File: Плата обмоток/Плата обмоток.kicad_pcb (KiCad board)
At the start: 2 copper layers, 58 x 58 mm, 7 parts, among them J1 A_OUT, J2 B_OUT, J3 C_OUT, J4 Conn_01x02, J5 Conn_02x02_Odd_Even, J6 Conn_01x02, J7 Conn_01x02

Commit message: Добавил ножевые разъёмы
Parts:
- added J10: 4900, Connector_My:3551, B.Cu at (70.9, 81.8)
- added J11: 4900, Connector_My:3551, B.Cu at (60.5, 99.1)
- added J12: 4900, Connector_My:3551, B.Cu at (61.9, 104.7)
- added J13: 4900, Connector_My:3551, B.Cu at (65.0, 109.8)
- added J8: 4900, Connector_My:3551, B.Cu at (78.8, 77.6)
- added J9: 4900, Connector_My:3551, B.Cu at (74.2, 78.4)
- J1: value A_OUT -> 4900; footprint Connector_My:Power_Wire -> Connector_My:3551; moved to B.Cu
- J2: value B_OUT -> 4900; footprint Connector_My:Power_Wire -> Connector_My:3551; moved to B.Cu
- J3: value C_OUT -> 4900; footprint Connector_My:Power_Wire -> Connector_My:3551; moved to B.Cu
- moved J3 39.3 mm to (96.5, 83.1), turned to 45 degrees
- moved J2 23.1 mm to (93.2, 79.7), turned to 60 degrees
- moved J1 4.19 mm to (88.8, 77.9), turned to 75 degrees
- moved J4 0.51 mm to (84.1, 116.1)
- moved J6 0.51 mm to (102.9, 94.7)
- moved J7 0.51 mm to (97.8, 109.2)
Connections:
- J2 pad 1: B_OUT -> A_OUT
- J3 pad 1: C_OUT -> A_OUT
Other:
- outline, holes or cut-outs redrawn

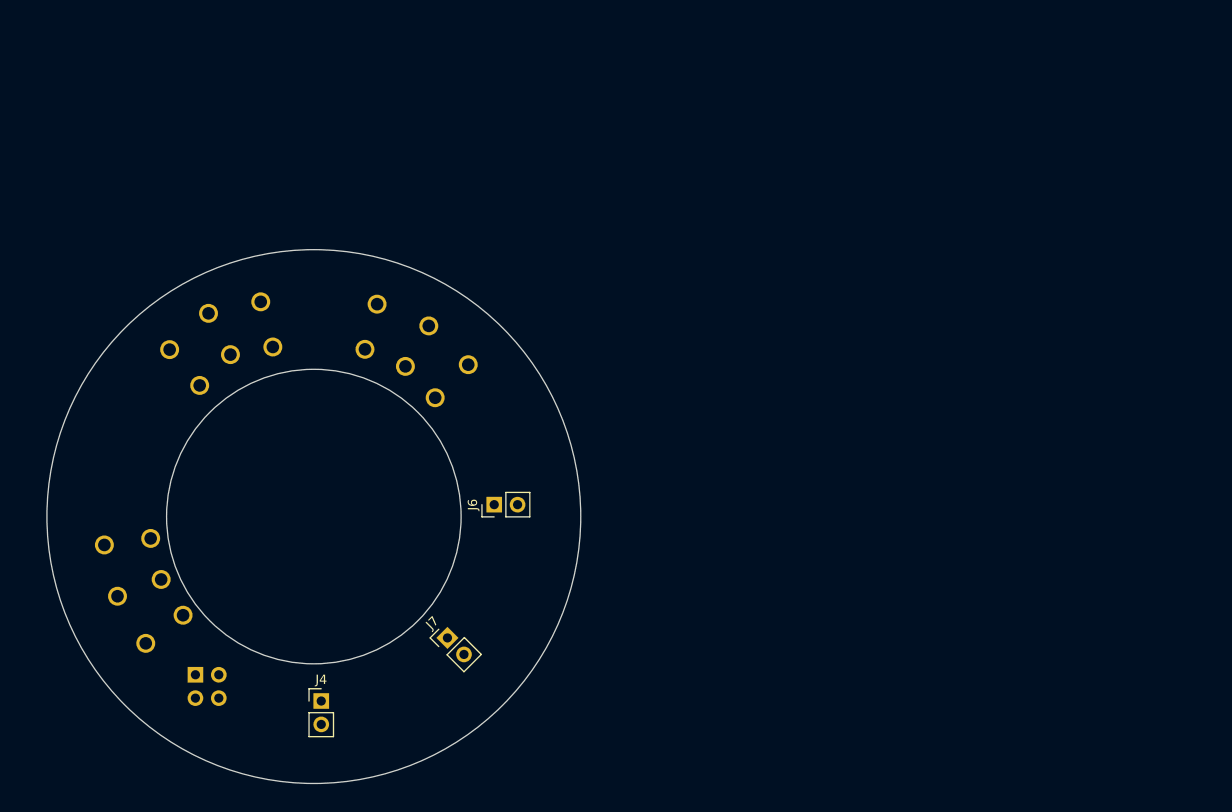
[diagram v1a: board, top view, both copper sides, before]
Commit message: Прямой вывод обмоток на плату
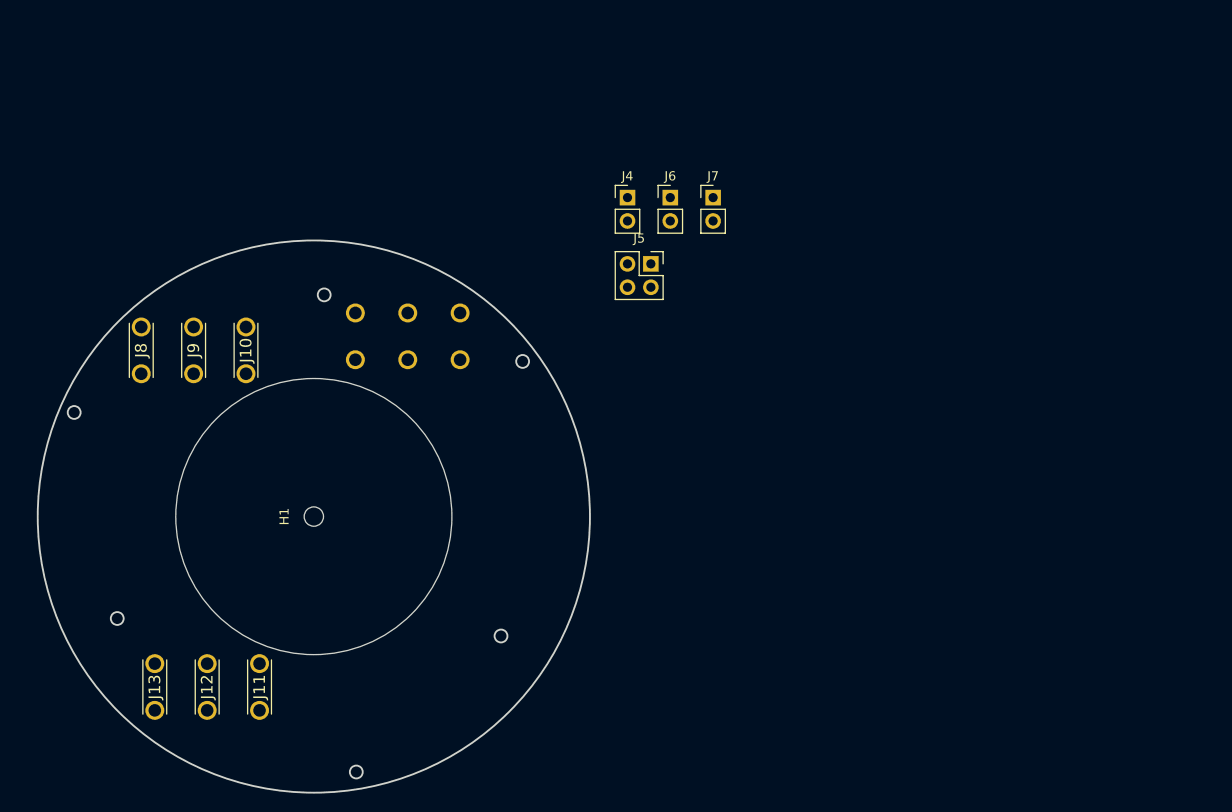
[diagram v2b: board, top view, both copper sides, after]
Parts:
- added H1: MountingHole, MountingHole:MountingHole_2.1mm, F.Cu at (83.3, 96.0)
- J10, J11, J12, J13, J5, J8, J9: moved to F.Cu
- moved J5 66.6 mm to (119.9, 68.6), turned to 0 degrees
- moved J4 64.0 mm to (117.3, 61.4)
- moved J7 55.9 mm to (126.6, 61.4), turned to 0 degrees
- moved J6 38.5 mm to (122.0, 61.4), turned to 0 degrees
- moved J11 21.2 mm to (77.4, 112.0), turned to -90 degrees
- moved J8 14.6 mm to (64.5, 80.5), turned to 90 degrees
- moved J12 12.2 mm to (71.7, 112.0), turned to -90 degrees
- moved J1 10.4 mm to (99.2, 79.0), turned to 90 degrees
- moved J3 9.60 mm to (87.8, 79.0), turned to 90 degrees
- moved J10 5.19 mm to (75.9, 80.5), turned to 90 degrees
- moved J9 4.51 mm to (70.2, 80.5), turned to 90 degrees
- moved J13 2.41 mm to (66.0, 112.0), turned to -90 degrees
- moved J2 0.77 mm to (93.5, 79.0), turned to 90 degrees
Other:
- board size 58 x 58 mm -> 60 x 60 mm
- board text added: "1"
- board text added: "2"
- board text added: "3"

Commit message: Расставил ножевые разъёмы финально
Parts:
- added J14: A1, Connector_My:Coil, F.Cu at (61.2, 86.4)
- added J15: A2, Connector_My:Coil, F.Cu at (87.1, 119.9)
- added J16: B1, Connector_My:Coil, F.Cu at (103.6, 109.0)
- added J17: B2, Connector_My:Coil, F.Cu at (102.6, 81.5)
- added J18: C1, Connector_My:Coil, F.Cu at (84.3, 71.9)
- added J19: C2, Connector_My:Coil, F.Cu at (62.0, 106.9)
- J10, J11, J12, J13, J5, J8, J9: moved to B.Cu
- moved J7 72.2 mm to (75.2, 112.0), turned to -25 degrees
- moved J5 67.2 mm to (67.0, 110.0), turned to 180 degrees
- moved J6 65.5 mm to (83.1, 114.0), turned to -5 degrees
- moved J4 64.7 mm to (79.0, 113.5), turned to -15 degrees
- moved J1 37.0 mm to (89.6, 114.7), turned to -70 degrees
- moved J2 33.3 mm to (94.2, 112.3), turned to -55 degrees
- moved J8 32.0 mm to (96.5, 82.1), turned to 45 degrees
- moved J3 31.4 mm to (98.0, 108.7), turned to -40 degrees
- moved J13 23.3 mm to (59.6, 89.6), turned to -15 degrees
- moved J9 22.3 mm to (92.5, 79.0), turned to 60 degrees
- moved J12 20.6 mm to (58.7, 96.0), turned to 0 degrees
- moved J11 20.2 mm to (59.6, 102.4), turned to 15 degrees
- moved J10 12.2 mm to (87.6, 77.1), turned to 75 degrees
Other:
- board size 60 x 60 mm -> 58 x 58 mm

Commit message: Финальная доработка
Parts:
- added H2: MountingHole, MountingHole:MountingHole_3.2mm_M3, F.Cu at (67.1, 81.3)
- added H3: MountingHole, MountingHole:MountingHole_3.2mm_M3, F.Cu at (80.8, 117.9)
- added H4: MountingHole, MountingHole:MountingHole_3.2mm_M3, F.Cu at (104.4, 89.9)
- J4, J6, J7: footprint Connector_PinHeader_2.54mm:PinHeader_1x02_P2.54mm_Vertical -> Connector_Molex:Molex_PicoBlade_53048-0210_1x02_P1.25mm_Horizontal; moved to B.Cu
- moved J6 40.1 mm to (72.1, 75.4), turned to -150 degrees
- moved J4 32.6 mm to (106.9, 96.6), turned to 90 degrees
- moved J7 5.76 mm to (72.3, 117.0), turned to -27 degrees
- turned J5 to 135 degrees
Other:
- outline, holes or cut-outs redrawn

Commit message: Ещё доработать
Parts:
- moved H3 43.9 mm to (90.2, 74.9)
- moved J9 43.8 mm to (71.9, 117.7)
- moved J5 43.3 mm to (97.8, 79.5)
- moved J8 42.8 mm to (76.7, 120.1), turned to 70 degrees
- moved J10 42.6 mm to (67.5, 114.7), turned to 50 degrees
- moved J17 41.7 mm to (61.2, 86.6)
- moved J15 40.1 mm to (103.6, 83.3)
- moved J6 36.3 mm to (105.4, 89.8), turned to 105 degrees
- moved J7 27.5 mm to (60.7, 92.1), turned to -95 degrees
- moved J19 27.3 mm to (85.9, 120.1)
- moved J11 25.6 mm to (67.0, 77.8), turned to -50 degrees
- moved J12 24.7 mm to (71.4, 74.8), turned to -60 degrees
- moved J13 23.9 mm to (76.3, 72.5), turned to -70 degrees
- moved J14 20.8 mm to (62.0, 107.2)
- moved H2 20.6 mm to (61.5, 101.1)
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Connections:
- J10 pad 1: B_OUT -> C_OUT
- J10 pad 2: B_OUT -> C_OUT
- J11 pad 1: C_OUT -> B_OUT
- J11 pad 2: C_OUT -> B_OUT
- J12 pad 1: C_OUT -> B_OUT
- J12 pad 2: C_OUT -> B_OUT
- J13 pad 1: C_OUT -> B_OUT
- J13 pad 2: C_OUT -> B_OUT
- J8 pad 1: B_OUT -> C_OUT
- J8 pad 2: B_OUT -> C_OUT
- J9 pad 1: B_OUT -> C_OUT
- J9 pad 2: B_OUT -> C_OUT
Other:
- board size 58 x 58 mm -> 61 x 58 mm

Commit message: Собираю документацию
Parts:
- removed H1: MountingHole, MountingHole:MountingHole_2.1mm
- moved J5 35.1 mm to (96.0, 114.6), turned to 180 degrees
- moved J1 26.3 mm to (109.7, 100.6), turned to 180 degrees
- moved J4 23.9 mm to (93.6, 76.3), turned to 155 degrees
- moved J3 23.9 mm to (109.7, 91.9), turned to 180 degrees
- moved J2 22.4 mm to (104.6, 96.3), turned to 0 degrees
- moved H4 22.1 mm to (88.4, 117.9)
- moved J6 9.29 mm to (100.5, 81.9), turned to 130 degrees
- moved J17 3.98 mm to (63.0, 83.1)
- moved J14 3.88 mm to (64.0, 110.5)
- moved J19 3.81 mm to (82.0, 120.1)
- moved H3 3.70 mm to (86.6, 73.9)
- moved J18 3.31 mm to (81.0, 72.1)
- moved J15 1.70 mm to (104.4, 84.8)
- moved J16 0.57 mm to (103.9, 108.5)
- moved J7 0.43 mm to (61.1, 92.1), turned to -100 degrees
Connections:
- J5 pad 2: PTC_Coil_C -> GNDA
- J5 pad 3: PTC_Coil_B -> PTC_Coil_C
- J5 pad 4: GNDA -> PTC_Coil_B
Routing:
- net PTC_Coil_C: track 0.00 -> 48.2 mm
- net PTC_Coil_A: track 0.00 -> 42.4 mm
- net PTC_Coil_B: track 0.00 -> 36.3 mm
- added copper zone on B.Cu, net A_OUT
- added copper zone on F.Cu, net A_OUT
- added copper zone on B.Cu, net B_OUT
- added copper zone on F.Cu, net B_OUT
- added copper zone on B.Cu, net C_OUT
- added copper zone on F.Cu, net C_OUT
- added copper zone on In2.Cu, net GNDA
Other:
- board size 61 x 58 mm -> 58 x 58 mm
- copper layers 2 -> 4
- board text removed: "1"
- board text removed: "3"

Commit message: Версия под отчётность
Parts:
- J14: renamed from J4; moved to F.Cu
- J16: renamed from J6; moved to F.Cu
- J19: renamed from J7; moved to F.Cu
- J5: renamed from J14; value A1 -> C2
- J6: renamed from J19; value C2 -> A1
- moved H3 15.5 mm to (101.4, 78.8)
- moved H2 12.3 mm to (59.3, 89.0)
- moved J16 9.98 mm to (96.3, 72.9), turned to -25 degrees
- moved J19 7.93 mm to (57.1, 98.9), turned to 100 degrees
- moved J14 7.51 mm to (89.2, 70.2), turned to -15 degrees
- moved J18 5.40 mm to (107.4, 104.4)
- moved J15 3.42 mm to (78.5, 69.8)
- moved J5 2.81 mm to (63.8, 113.3)
- moved H1 2.59 mm to (89.1, 120.3)
- renumbered H4 to H1, J12 to J10, J3 to J11, J10 to J12, J18 to J15, J15 to J17, J16 to J18, J8 to J2, J11 to J3, J5 to J4, J17 to J7, J2 to J8
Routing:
- net PTC_Coil_B: track 36.3 -> 48.8 mm
- net PTC_Coil_A: track 42.4 -> 52.2 mm
- net PTC_Coil_C: track 48.2 -> 49.9 mm
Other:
- outline, holes or cut-outs redrawn
- board text removed: "2"

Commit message: VER2.0
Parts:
- added J20: B1, Connector_My:temp_wire, B.Cu at (156.2, 97.3)
- added J21: B1, Connector_My:temp_wire, B.Cu at (145.4, 97.3)
- J14: value Conn_01x02 -> Conn_01x03; footprint Connector_Molex:Molex_PicoBlade_53048-0210_1x02_P1.25mm_Horizontal -> Connector_PinSocket_2.54mm:PinSocket_1x03_P2.54mm_Vertical; moved to B.Cu
- J15, J17, J18, J5, J6, J7: moved to B.Cu
- J16: value Conn_01x02 -> 4900; footprint Connector_Molex:Molex_PicoBlade_53048-0210_1x02_P1.25mm_Horizontal -> Connector_My:3551; moved to B.Cu
- J19: value Conn_01x02 -> B1; footprint Connector_Molex:Molex_PicoBlade_53048-0210_1x02_P1.25mm_Horizontal -> Connector_My:temp_wire; moved to B.Cu
- J4: value Conn_02x02_Odd_Even -> B1; footprint Connector_PinSocket_2.54mm:PinSocket_2x02_P2.54mm_Vertical -> Connector_My:temp_wire
- moved H2 116.3 mm to (171.4, 58.4)
- moved J3 101.7 mm to (165.9, 54.4), turned to 90 degrees
- moved J7 100.5 mm to (156.5, 46.2), turned to 180 degrees
- moved J10 92.3 mm to (161.4, 54.4), turned to 90 degrees
- moved J19 85.8 mm to (142.9, 97.3), turned to 0 degrees
- moved J14 79.4 mm to (165.9, 90.6), turned to 90 degrees
- moved J5 78.1 mm to (124.6, 64.3), turned to -90 degrees
- moved J18 78.0 mm to (174.4, 64.3), turned to 90 degrees
- moved J8 71.9 mm to (174.1, 77.9), turned to 180 degrees
- moved J17 71.7 mm to (174.2, 68.8), turned to 90 degrees
- moved J12 70.5 mm to (124.6, 73.5), turned to 0 degrees
- moved J15 67.8 mm to (142.0, 46.2), turned to 180 degrees
- moved J11 67.0 mm to (174.1, 73.5)
- moved J1 67.0 mm to (174.1, 82.4)
- moved J6 66.7 mm to (124.6, 68.8), turned to -90 degrees
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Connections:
- net A_OUT renamed A
- net C_OUT renamed C
- J10 pad 1: B_OUT -> B
- J10 pad 2: B_OUT -> B
- J13 pad 1: B_OUT -> B
- J13 pad 2: B_OUT -> B
- J14 pad 2: GNDA -> PTC_Coil_B
- J15 pad 1: B_OUT -> B
- J16 pad 1: PTC_Coil_B -> B
- J16 pad 2: GNDA -> B
- J19 pad 1: PTC_Coil_C -> PTC_Coil_B
- J3 pad 1: B_OUT -> B
- J3 pad 2: B_OUT -> B
- J7 pad 1: B_OUT -> B
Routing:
- net PTC_Coil_C: track 49.9 -> 0.00 mm
- net PTC_Coil_A: track 52.2 -> 15.0 mm
- net PTC_Coil_B: track 48.8 -> 25.0 mm
- added copper zone on In1.Cu, net A
- added copper zone on In2.Cu, net A
- added copper zone on B.Cu, net B
- added copper zone on F.Cu, net B
- added copper zone on In1.Cu, net B
- added copper zone on In2.Cu, net B
- added copper zone on In1.Cu, net C
- added copper zone on In2.Cu, net C
- removed copper zone on B.Cu, net B_OUT
- removed copper zone on F.Cu, net B_OUT
